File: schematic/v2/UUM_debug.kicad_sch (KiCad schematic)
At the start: 16 parts, among them J16 DSM_DBG, J20 USB_A, U33 CH340G, Y2 Crystal

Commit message: no errors in the ERC!
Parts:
- removed C14, C15, C16: 22pf, Capacitor_SMD:C_0805_2012Metric, symbol Device:C_Small
- removed D39, D50: LED_PWR, LED_SMD:LED_0603_1608Metric, symbol Device:LED
- removed D40: TXD, LED_SMD:LED_0603_1608Metric, symbol Device:LED
- removed D41: RXD, LED_SMD:LED_0603_1608Metric, symbol Device:LED
- removed J16: DSM_DBG, Connector_PinHeader_1.00mm:PinHeader_1x03_P1.00mm_Horizontal, symbol Connector_Generic:Conn_01x03
- removed J20: USB_A, Connector_USB:USB_A_CNCTech_1001-011-01101_Horizontal, symbol Connector:USB_A
- removed R57, R58, R59, R60: 300, Resistor_SMD:R_0805_2012Metric_Pad1.20x1.40mm_HandSolder, symbol Device:R
- removed R61: 1k5, Resistor_SMD:R_0805_2012Metric_Pad1.20x1.40mm_HandSolder, symbol Device:R
- removed U33: CH340G, Package_SO:SOIC-16_3.9x9.9mm_P1.27mm, symbol Interface_USB:CH340G
- removed Y2: Crystal, symbol Device:Crystal
- added C20, C21, C22: 22pf, Capacitor_SMD:C_0805_2012Metric, symbol Device:C_Small
- added D46, D47: LED_PWR, LED_SMD:LED_0603_1608Metric, symbol Device:LED
- added D48: TXD, LED_SMD:LED_0603_1608Metric, symbol Device:LED
- added D49: RXD, LED_SMD:LED_0603_1608Metric, symbol Device:LED
- added J13: UUM_DBG, Connector_PinHeader_1.00mm:PinHeader_1x03_P1.00mm_Horizontal, symbol Connector_Generic:Conn_01x03
- added J24: USB_A, Connector_USB:USB_A_CNCTech_1001-011-01101_Horizontal, symbol Connector:USB_A
- added R67, R68, R69, R70: 300, Resistor_SMD:R_0805_2012Metric_Pad1.20x1.40mm_HandSolder, symbol Device:R
- added R71: 1k5, Resistor_SMD:R_0805_2012Metric_Pad1.20x1.40mm_HandSolder, symbol Device:R
- added U35: CH340G, Package_SO:SOIC-16_3.9x9.9mm_P1.27mm, symbol Interface_USB:CH340G
- added Y4: Crystal, symbol Device:Crystal
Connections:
- net GND: now also C21.2, C22.2, D46.1 (K), D47.1 (K), D48.1 (K), D49.1 (K), J13.3 (Pin_3), J24.4 (GND), U35.1 (GND), Y4.1, Y4.2
- new net: C21.1, U35.7 (XI)
- new net: J24.2 (D-), U35.6 (UD-)
- new net: J24.3 (D+), U35.5 (UD+)
- new net: D49.2 (A), R70.2
- new net: D48.2 (A), R69.2
- new net: D47.2 (A), R68.1
- new net: C22.1, U35.8 (XO)
- new net: D46.2 (A), R67.1
- new net UUM_DBG_RX: J13.2 (Pin_2), R69.1, R70.1, R71.1, U35.2 (TXD), U35.3 (RXD)
- new net UUM_DBG_TX: J13.1 (Pin_1), R71.2
- new net UUM_VDD: C20.2, J24.1 (VBUS), R67.2, R68.2, U35.16 (VCC)
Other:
- note added: "UUM Debug Port"
- note added: "UUM USB2.0 DBG PORT"
- note removed: "DSM Debug Port"
- note removed: "DSM USB2.0 DBG PORT"

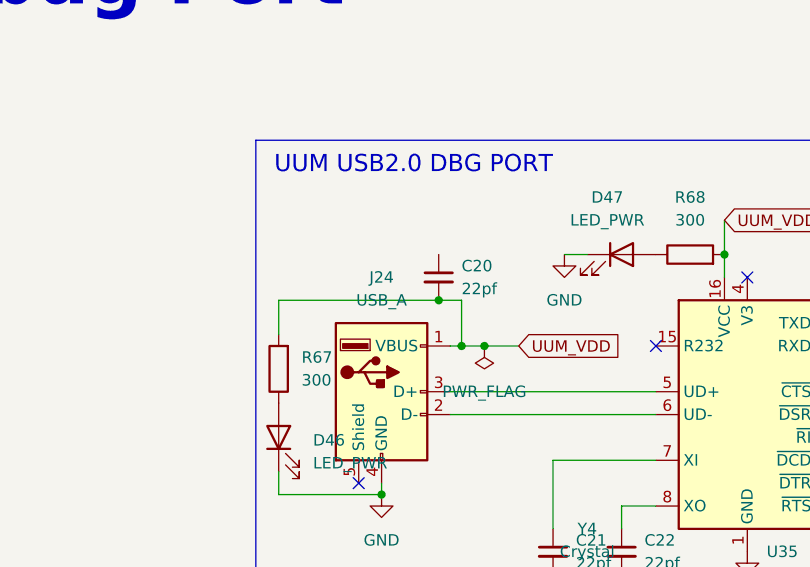
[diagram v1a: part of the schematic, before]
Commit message: need to update PCB and new traces
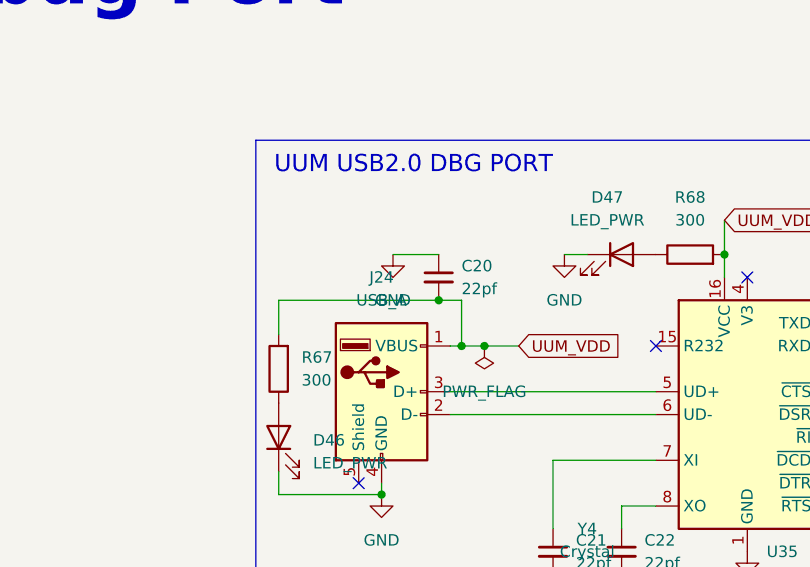
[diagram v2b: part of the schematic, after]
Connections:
- net GND: now also C20.1
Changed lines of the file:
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@@
+	(wire
+		(pts
+			(xy 97.79 49.53) (xy 102.87 49.53)
+		)
+		(stroke
+			(width 0)
+			(type default)
+		)
+	)
 	(wire
 		(pts
@@
 		(on_board yes)
 		(dnp no)
-		(fields_autoplaced yes)
 		(property "Reference" "J24"
 			(at 96.52 52.07 0)
@@
 					(unit 1)
 				)
+			)
+		)
+	)
+	(symbol
+		(lib_id "power:GND")
+		(at 97.79 49.53 0)
+		(unit 1)
+		(exclude_from_sim no)
+		(in_bom yes)
+		(on_board yes)
+		(dnp no)
+		(fields_autoplaced yes)
+		(property "Reference" "#PWR0104"
+			(at 97.79 55.88 0)
+			(effects
+				(font
+					(size 1.27 1.27)
+				)
+				(hide yes)
+			)
+		)
+		(property "Value" "GND"
+			(at 97.79 54.61 0)
+			(effects
+				(font
+					(size 1.27 1.27)
+				)
+			)
+		)
+		(property "Footprint" ""
+			(at 97.79 49.53 0)
+			(effects
+				(font
+					(size 1.27 1.27)
+				)
+				(hide yes)
+			)
+		)
+		(property "Datasheet" ""
+			(at 97.79 49.53 0)
+			(effects
+				(font
+					(size 1.27 1.27)
+				)
+				(hide yes)
+			)
+		)
+		(property "Description" "Power symbol creates a global label with name \"GND\" , ground"
+			(at 97.79 49.53 0)
+			(effects
+				(font
+					(size 1.27 1.27)
+				)
+				(hide yes)
+			)
+		)
+		(pin "1"
+		)
+		(instances
+			(project "signalmesh"
+				(path "/fe7b15e9-f0ed-4338-9f03-dd7651dace13/e0c3e94a-d1d6-4c70-a171-e825d34fc315/6ca91b78-c21d-453e-b265-69dc1e96013e"
+					(reference "#PWR0104")
+					(unit 1)
+				)
